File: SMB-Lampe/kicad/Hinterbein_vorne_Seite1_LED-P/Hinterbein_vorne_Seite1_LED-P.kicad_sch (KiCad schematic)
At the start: 1 part

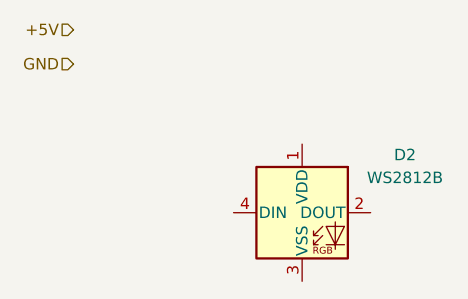
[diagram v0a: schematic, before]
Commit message: Hauptplatine skizziert
Bezeichner stimmen noch nicht
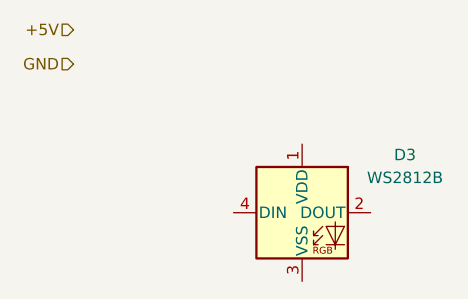
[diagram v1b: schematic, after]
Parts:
- renumbered D2 to D3
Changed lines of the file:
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@@
 		(dnp no)
 		(fields_autoplaced yes)
-		(property "Reference" "D2"
+		(property "Reference" "D3"
 			(at 62.23 39.2998 0)
 			(effects
@@
 			(project "SMB-Lampe"
 				(path "/4831ca1b-de6c-4f01-b2f4-c7955e9e85c5/cf45c117-84b0-4357-8470-1c2bf47a1b84"
-					(reference "D2")
+					(reference "D3")
 					(unit 1)
 				)

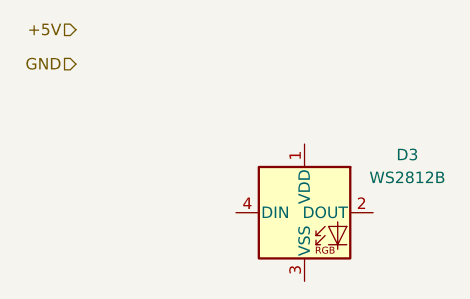
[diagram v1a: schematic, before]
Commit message: Alle Platinen erstellt
Alle Platinen wurden im Projekt einzeln erstellt.
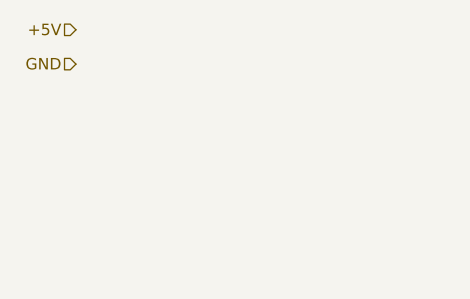
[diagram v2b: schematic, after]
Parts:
- removed D3: WS2812B, LED_SMD:LED_WS2812B_PLCC4_5.0x5.0mm_P3.2mm, symbol LED:WS2812B
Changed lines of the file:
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@@
-		)
-	)
-	(symbol
-		(lib_id "LED:WS2812B")
-		(at 50.8 45.72 0)
-		(unit 1)
-		(exclude_from_sim no)
-		(in_bom yes)
-		(on_board yes)
-		(dnp no)
-		(fields_autoplaced yes)
-		(property "Reference" "D3"
-			(at 62.23 39.2998 0)
-			(effects
-				(font
-					(size 1.27 1.27)
-				)
-			)
-		)
-		(property "Value" "WS2812B"
-			(at 62.23 41.8398 0)
-			(effects
-				(font
-					(size 1.27 1.27)
-				)
-			)
-		)
-		(property "Footprint" "LED_SMD:LED_WS2812B_PLCC4_5.0x5.0mm_P3.2mm"
-			(at 52.07 53.34 0)
-			(effects
-				(font
-					(size 1.27 1.27)
-				)
-				(justify left top)
-				(hide yes)
-			)
-		)
-		(property "Datasheet" "https://cdn-shop.adafruit.com/datasheets/WS2812B.pdf"
-			(at 53.34 55.245 0)
-			(effects
-				(font
-					(size 1.27 1.27)
-				)
-				(justify left top)
-				(hide yes)
-			)
-		)
-		(property "Description" "RGB LED with integrated controller"
-			(at 50.8 45.72 0)
-			(effects
-				(font
-					(size 1.27 1.27)
-				)
-				(hide yes)
-			)
-		)
-		(pin "1"
-		)
-		(pin "3"
-		)
-		(pin "2"
-		)
-		(pin "4"
-		)
-		(instances
-			(project "SMB-Lampe"
-				(path "/4831ca1b-de6c-4f01-b2f4-c7955e9e85c5/cf45c117-84b0-4357-8470-1c2bf47a1b84"
-					(reference "D3")
-					(unit 1)
-				)
-			)
 		)
 	)

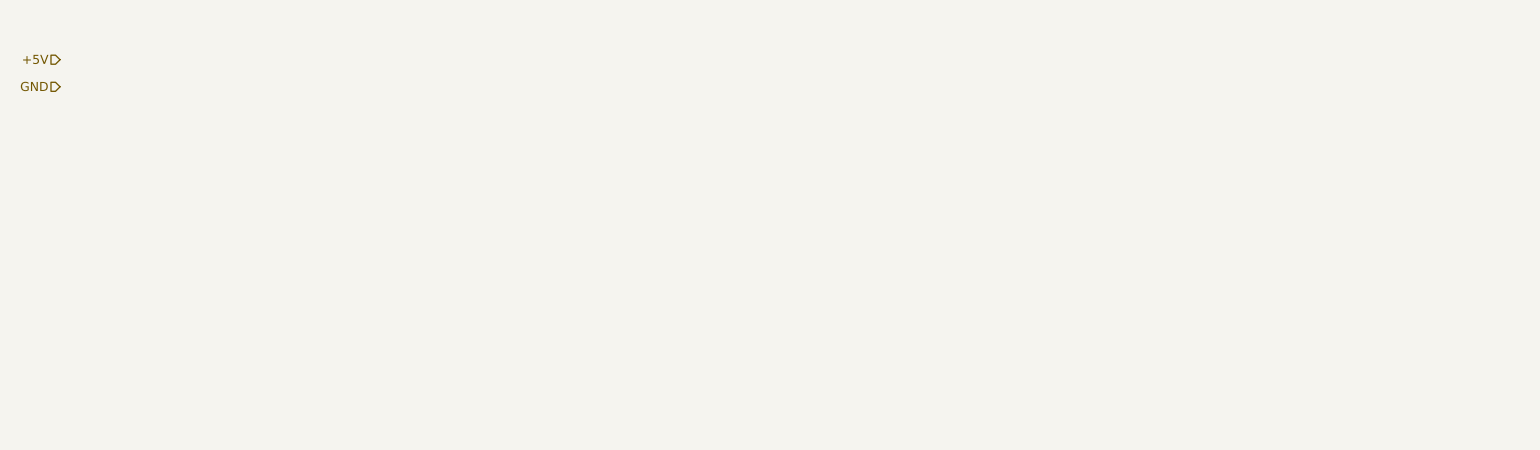
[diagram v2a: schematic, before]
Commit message: Vorderes Hinterbein fertig
Alle Platinen sind fertig beschaltet
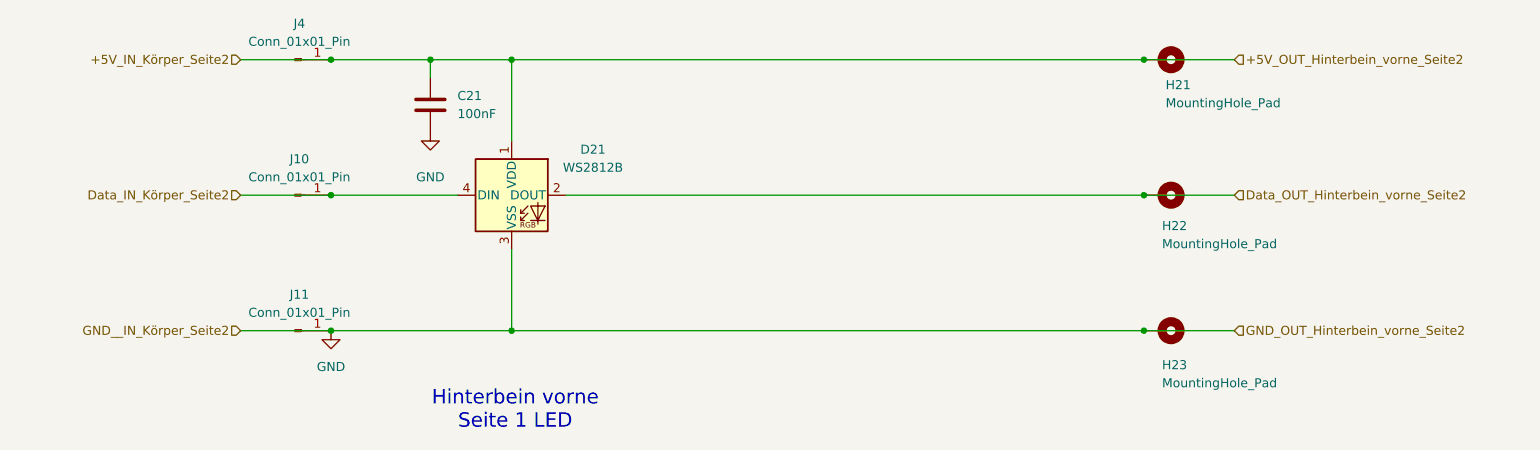
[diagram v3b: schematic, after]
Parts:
- added C21: 100nF, Capacitor_SMD:C_0201_0603Metric, symbol Device:C
- added D21: WS2812B, LED_SMD:LED_WS2812B_PLCC4_5.0x5.0mm_P3.2mm, symbol LED:WS2812B
- added H21, H22, H23: MountingHole_Pad, Eigenen_Library:MountingHole D2 x d1 test, symbol Mechanical:MountingHole_Pad
- added J10, J11, J4: Conn_01x01_Pin, TestPoint:TestPoint_Pad_2.0x2.0mm, symbol Connector:Conn_01x01_Pin
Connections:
- net GND: now also C21.2, D21.3 (VSS), H23.1, J11.1 (Pin_1)
- new net +5V_IN_Körper_Seite2: C21.1, D21.1 (VDD), H21.1, J4.1 (Pin_1)
- new net Data_IN_Körper_Seite2: D21.4 (DIN), J10.1 (Pin_1)
- new net Data_OUT_Hinterbein_vorne_Seite2: D21.2 (DOUT), H22.1
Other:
- note added: "Hinterbein vorne Seite 1 LED"

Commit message: Hinterbeine Geändert teilweiße Körper
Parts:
- C21: footprint Capacitor_SMD:C_0201_0603Metric -> Capacitor_SMD:C_0603_1608Metric_Pad1.08x0.95mm_HandSolder
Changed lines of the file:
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@@
 			)
 		)
-		(property "Footprint" "Capacitor_SMD:C_0201_0603Metric"
+		(property "Footprint" "Capacitor_SMD:C_0603_1608Metric_Pad1.08x0.95mm_HandSolder"
 			(at 78.4352 35.56 0)
 			(effects

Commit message: vor Schaltplananpassung
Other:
- note added: "LED Hinterbein vorne Seite 1"
- note removed: "Hinterbein vorne Seite 1 LED"
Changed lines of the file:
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@@
 		(company "IFM")
 	)
-	(text "Hinterbein vorne\nSeite 1 LED"
+	(text "LED Hinterbein vorne\nSeite 1 "
 		(exclude_from_sim no)
 		(at 89.408 74.676 0)

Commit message: Änderungen für Dokumentation
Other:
- company: IFM -> IFM / Lukas Gulde
- title: (none) -> Projektaarbeit SMB-Lampe
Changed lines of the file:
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@@
 	(paper "A4")
 	(title_block
-		(company "IFM")
+		(title "Projektaarbeit SMB-Lampe")
+		(date "2026-03-31")
+		(company "IFM / Lukas Gulde")
 	)
 	(text "LED Hinterbein vorne\nSeite 1 "
